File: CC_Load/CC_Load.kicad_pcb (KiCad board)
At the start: 2 copper layers, 160 x 120 mm, 8 parts

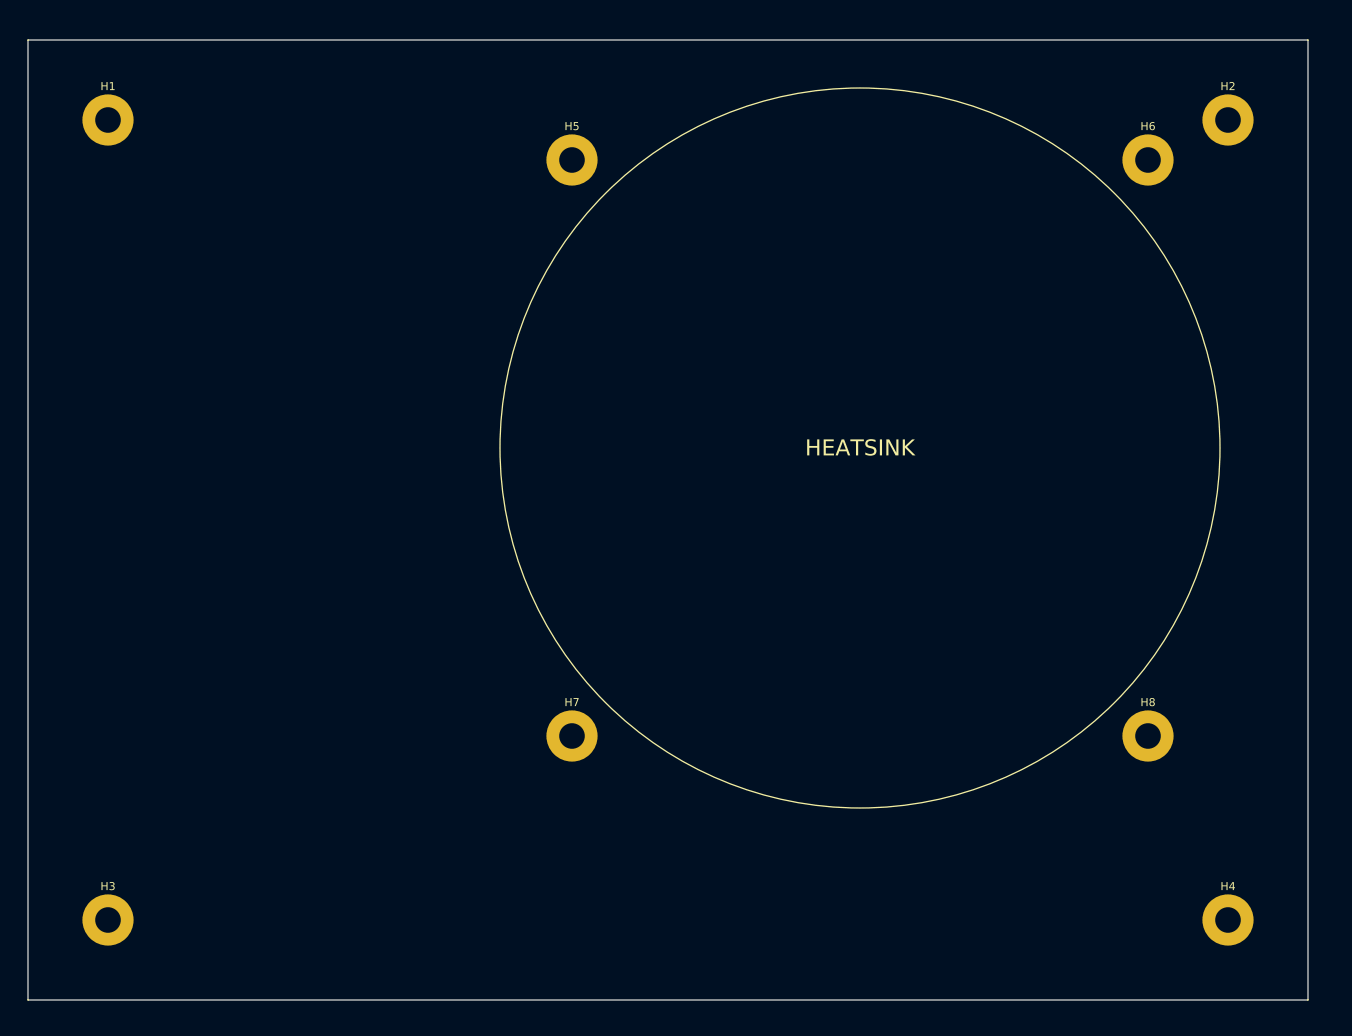
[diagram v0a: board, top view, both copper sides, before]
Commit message: Finished first design for my DIY PCB
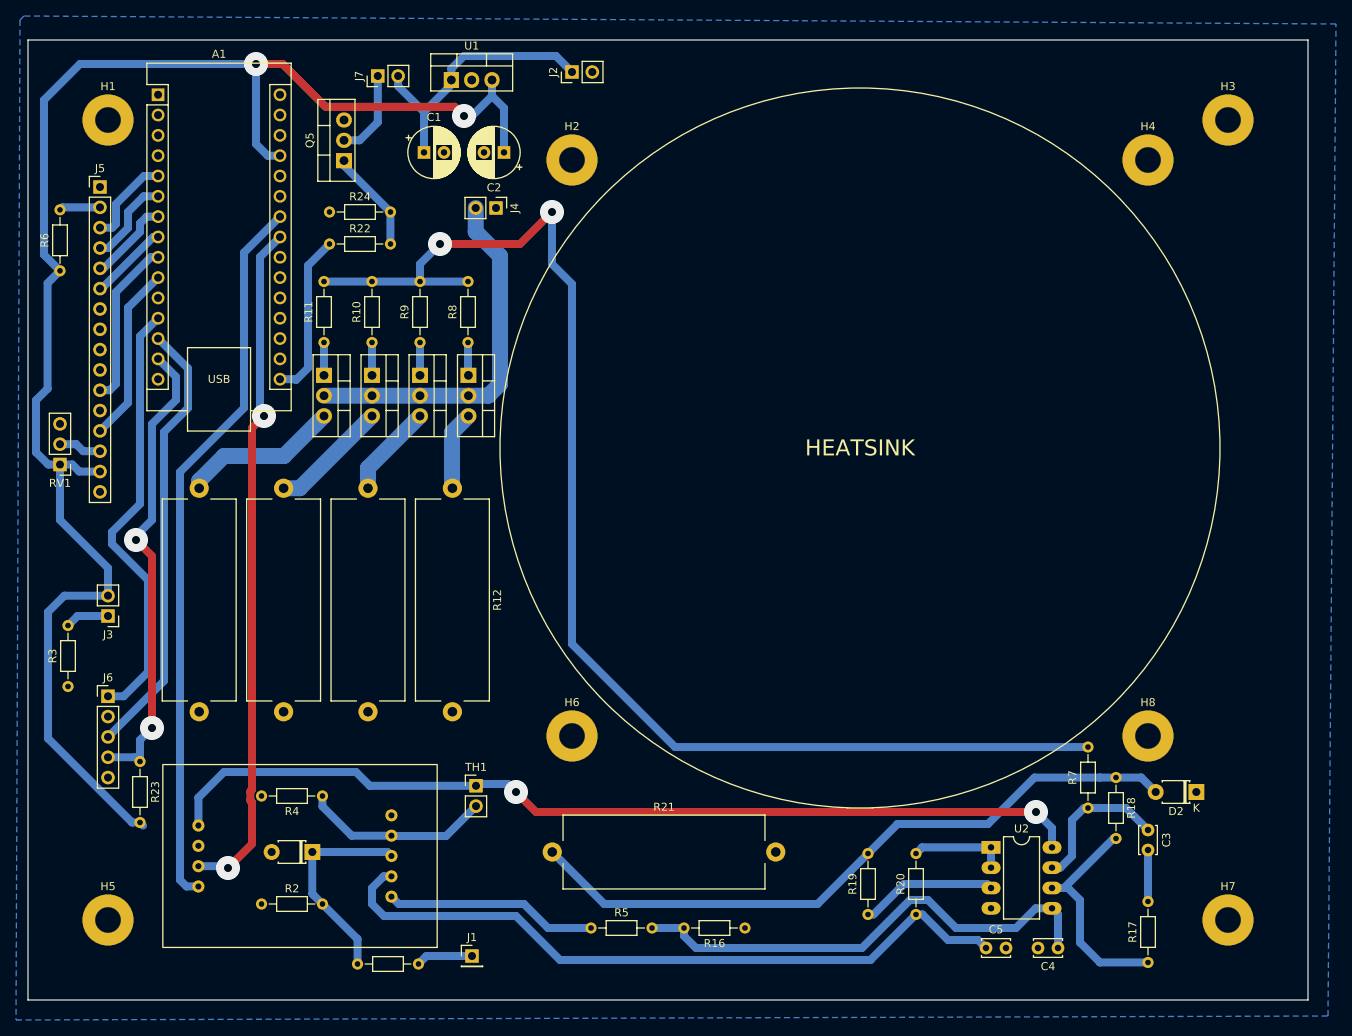
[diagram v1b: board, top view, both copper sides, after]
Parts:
- added A1: Arduino_Nano, Module:Arduino_Nano, F.Cu at (66.3, 36.8)
- added A2: ~, MyFootprintLibrary:ADC_DAC_Board, F.Cu at (84.0, 132.0)
- added C1: 100uF, Capacitor_THT:CP_Radial_D6.3mm_P2.50mm, F.Cu at (99.5, 44.1)
- added C2: 100uF, Capacitor_THT:CP_Radial_D6.3mm_P2.50mm, F.Cu at (109.5, 44.1)
- added C3: 1n, Capacitor_THT:C_Disc_D3.4mm_W2.1mm_P2.50mm, F.Cu at (190.0, 128.8)
- added C4: 100nF, Capacitor_THT:C_Disc_D3.4mm_W2.1mm_P2.50mm, F.Cu at (178.8, 143.5)
- added C5: 100n, Capacitor_THT:C_Disc_D3.4mm_W2.1mm_P2.50mm, F.Cu at (169.8, 143.5)
- added D1: 5V, Diode_THT:D_T-1_P5.08mm_Horizontal, F.Cu at (85.5, 131.5)
- added D2: D, Diode_THT:D_T-1_P5.08mm_Horizontal, F.Cu at (196.0, 124.0)
- added J1: VoltSense_Conn, Connector_PinHeader_2.54mm:PinHeader_1x01_P2.54mm_Vertical, F.Cu at (105.5, 144.5)
- added J2: PowerInput_Conn, Connector_PinHeader_2.54mm:PinHeader_1x02_P2.54mm_Vertical, F.Cu at (118.0, 34.0)
- added J3: LED_Conn, Connector_PinHeader_2.54mm:PinHeader_1x02_P2.54mm_Vertical, F.Cu at (60.0, 102.0)
- added J4: Load_Conn, Connector_PinHeader_2.54mm:PinHeader_1x02_P2.54mm_Vertical, F.Cu at (108.5, 51.0)
- added J5: 16x2_LCD_Conn, Connector_PinHeader_2.54mm:PinHeader_1x16_P2.54mm_Vertical, F.Cu at (59.0, 48.4)
- added J6: RotEnc_Conn, Connector_PinHeader_2.54mm:PinHeader_1x05_P2.54mm_Vertical, F.Cu at (60.0, 112.0)
- added J7: Fan_Conn, Connector_PinHeader_2.54mm:PinHeader_1x02_P2.54mm_Vertical, F.Cu at (93.7, 34.5)
- added Q1: IRLZ44N, Package_TO_SOT_THT:TO-220-3_Vertical, F.Cu at (105.1, 71.9)
- added Q2: IRLZ44N, Package_TO_SOT_THT:TO-220-3_Vertical, F.Cu at (99.0, 71.9)
- added Q3: IRLZ44N, Package_TO_SOT_THT:TO-220-3_Vertical, F.Cu at (93.0, 71.9)
- added Q4: IRLZ44N, Package_TO_SOT_THT:TO-220-3_Vertical, F.Cu at (87.0, 71.9)
- added Q5: IRLZ44N, Package_TO_SOT_THT:TO-220-3_Vertical, F.Cu at (89.5, 45.1)
- added R1: 39k, Resistor_THT:R_Axial_DIN0204_L3.6mm_D1.6mm_P7.62mm_Horizontal, F.Cu at (91.2, 145.5)
- added R10: 100R, Resistor_THT:R_Axial_DIN0204_L3.6mm_D1.6mm_P7.62mm_Horizontal, F.Cu at (93.0, 67.8)
- added R11: 100R, Resistor_THT:R_Axial_DIN0204_L3.6mm_D1.6mm_P7.62mm_Horizontal, F.Cu at (87.0, 67.8)
- added R12: 0.1R, Resistor_THT:R_Axial_Power_L25.0mm_W9.0mm_P27.94mm, F.Cu at (103.0, 86.0)
- added R13: 0.1R, Resistor_THT:R_Axial_Power_L25.0mm_W9.0mm_P27.94mm, F.Cu at (92.5, 86.0)
- added R14: 0.1R, Resistor_THT:R_Axial_Power_L25.0mm_W9.0mm_P27.94mm, F.Cu at (82.0, 86.0)
- added R15: 0.1R, Resistor_THT:R_Axial_Power_L25.0mm_W9.0mm_P27.94mm, F.Cu at (71.4, 86.0)
- added R16: 1k, Resistor_THT:R_Axial_DIN0204_L3.6mm_D1.6mm_P7.62mm_Horizontal, F.Cu at (139.6, 141.0)
- added R17: 1k, Resistor_THT:R_Axial_DIN0204_L3.6mm_D1.6mm_P7.62mm_Horizontal, F.Cu at (190.0, 145.3)
- added R18: 10k, Resistor_THT:R_Axial_DIN0204_L3.6mm_D1.6mm_P7.62mm_Horizontal, F.Cu at (186.0, 122.2)
- added R19: 10k, Resistor_THT:R_Axial_DIN0204_L3.6mm_D1.6mm_P7.62mm_Horizontal, F.Cu at (155.0, 139.3)
- added R2: 10k, Resistor_THT:R_Axial_DIN0204_L3.6mm_D1.6mm_P7.62mm_Horizontal, F.Cu at (79.2, 138.0)
- added R20: 100R, Resistor_THT:R_Axial_DIN0204_L3.6mm_D1.6mm_P7.62mm_Horizontal, F.Cu at (161.0, 139.3)
- added R21: 0.1R, Resistor_THT:R_Axial_Power_L25.0mm_W9.0mm_P27.94mm, F.Cu at (115.5, 131.5)
- added R22: 220R, Resistor_THT:R_Axial_DIN0204_L3.6mm_D1.6mm_P7.62mm_Horizontal, F.Cu at (87.7, 55.5)
- added R23: 10k, Resistor_THT:R_Axial_DIN0204_L3.6mm_D1.6mm_P7.62mm_Horizontal, F.Cu at (64.0, 120.2)
- added R24: 10k, Resistor_THT:R_Axial_DIN0204_L3.6mm_D1.6mm_P7.62mm_Horizontal, F.Cu at (87.7, 51.5)
- added R3: 220R, Resistor_THT:R_Axial_DIN0204_L3.6mm_D1.6mm_P7.62mm_Horizontal, F.Cu at (55.0, 110.8)
- added R4: 10k, Resistor_THT:R_Axial_DIN0204_L3.6mm_D1.6mm_P7.62mm_Horizontal, F.Cu at (86.8, 124.5)
- added R5: 10k, Resistor_THT:R_Axial_DIN0204_L3.6mm_D1.6mm_P7.62mm_Horizontal, F.Cu at (120.4, 141.0)
- added R6: 470R, Resistor_THT:R_Axial_DIN0204_L3.6mm_D1.6mm_P7.62mm_Horizontal, F.Cu at (54.0, 58.9)
- added R7: 100R, Resistor_THT:R_Axial_DIN0204_L3.6mm_D1.6mm_P7.62mm_Horizontal, F.Cu at (182.5, 126.0)
- added R8: 100R, Resistor_THT:R_Axial_DIN0204_L3.6mm_D1.6mm_P7.62mm_Horizontal, F.Cu at (105.0, 67.8)
- added R9: 100R, Resistor_THT:R_Axial_DIN0204_L3.6mm_D1.6mm_P7.62mm_Horizontal, F.Cu at (99.0, 67.8)
- added RV1: 10k, Connector_PinHeader_2.54mm:PinHeader_1x03_P2.54mm_Vertical, F.Cu at (54.0, 83.1)
- added TH1: 10k_NTC, Connector_PinHeader_2.54mm:PinHeader_1x02_P2.54mm_Vertical, F.Cu at (106.0, 123.2)
- added U1: LM7805_TO220, Package_TO_SOT_THT:TO-220-3_Vertical, F.Cu at (102.9, 35.0)
- added U2: LM358, Package_DIP:DIP-8_W7.62mm_LongPads, F.Cu at (170.4, 130.9)
- renumbered H5 to H2, H2 to H3, H6 to H4, H3 to H5, H7 to H6, H4 to H7
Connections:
- H1 pad 1: unconnected-(H1-Pad1) -> GND
- H2 pad 1: unconnected-(H5-Pad1) -> GND
- H3 pad 1: unconnected-(H2-Pad1) -> GND
- H4 pad 1: unconnected-(H6-Pad1) -> GND
- H5 pad 1: unconnected-(H3-Pad1) -> GND
- H6 pad 1: unconnected-(H7-Pad1) -> GND
- H7 pad 1: unconnected-(H4-Pad1) -> GND
- H8 pad 1: unconnected-(H8-Pad1) -> GND
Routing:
- net +5V: track 0.00 -> 316.6 mm, vias 0 -> 4
- net Net-(R10-Pad2): track 0.00 -> 164.3 mm, vias 0 -> 2
- net Net-(A1-SCL/A5): track 0.00 -> 90.7 mm
- net curr_sense: track 0.00 -> 88.8 mm
- net Net-(A1-SDA/A4): track 0.00 -> 86.0 mm, vias 0 -> 2
- net Net-(D2-A): track 0.00 -> 85.4 mm
- net Net-(U2B-+): track 0.00 -> 61.8 mm
- net Net-(A1-MOSI): track 0.00 -> 59.0 mm, vias 0 -> 2
- net Net-(A1-D10): track 0.00 -> 55.5 mm
- net Net-(A1-D9): track 0.00 -> 54.7 mm
- net Net-(J4-Pin_2): track 0.00 -> 45.9 mm
- net +12V: track 0.00 -> 34.3 mm
- net Net-(U2B--): track 0.00 -> 29.5 mm
- net curr_set: track 0.00 -> 26.6 mm
- net volt_sense: track 0.00 -> 26.4 mm
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- added copper zone on B.Cu, net GND

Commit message: Changed PCB design, will order from JLCPCB
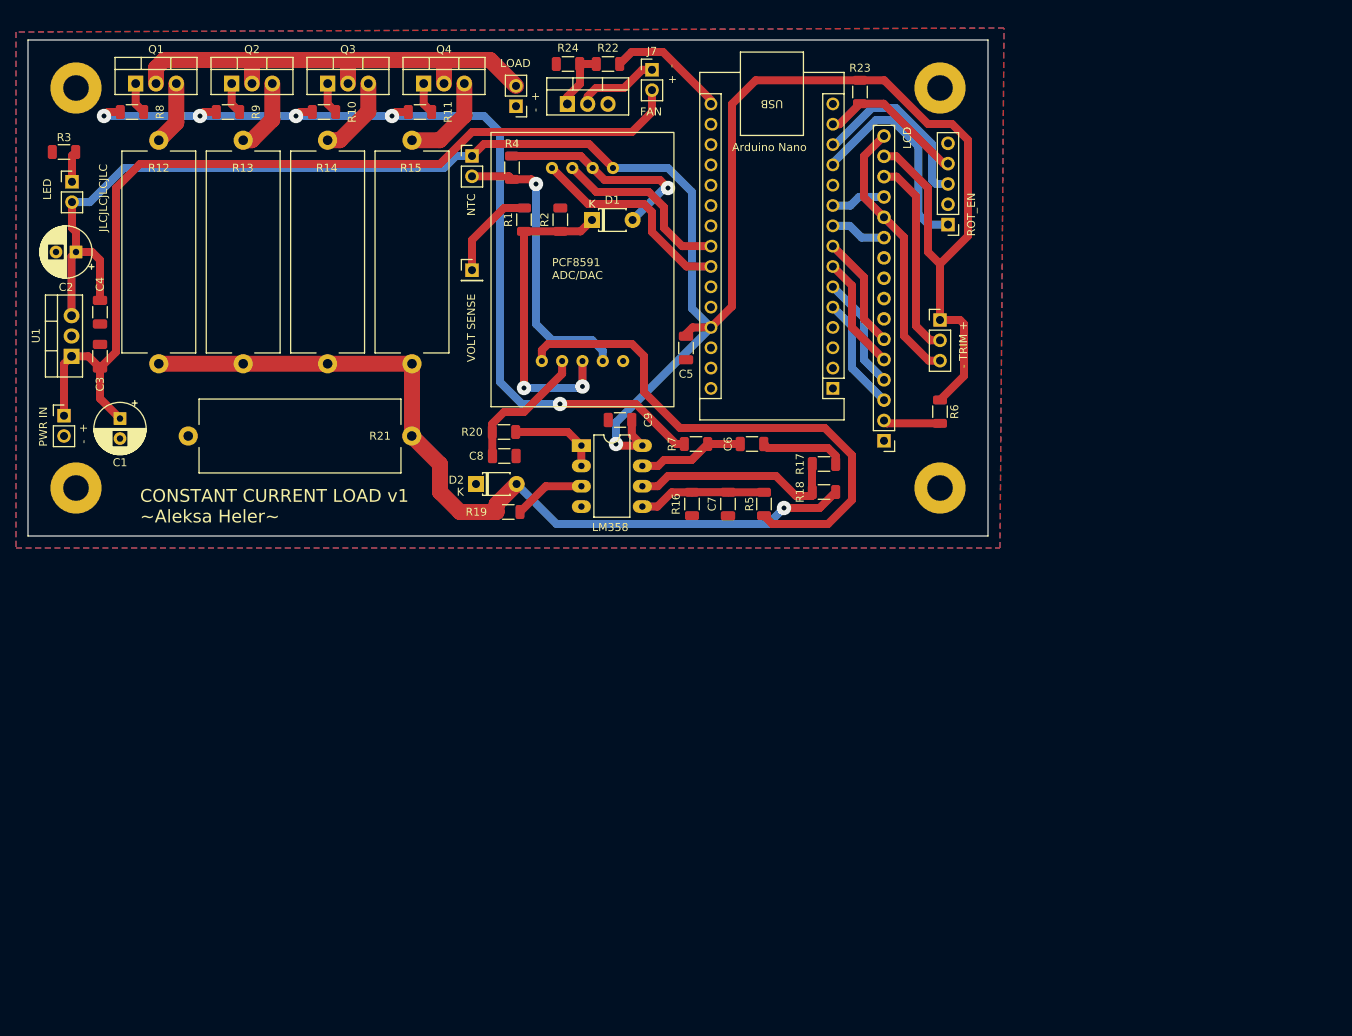
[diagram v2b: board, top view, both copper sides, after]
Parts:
- removed H5, H6, H7, H8: MountingHole_Pad, MountingHole:MountingHole_3.2mm_M3_Pad
- added C6: 1nF, Capacitor_SMD:C_1206_3216Metric, F.Cu at (140.5, 80.5)
- added C7: 100nF, Capacitor_SMD:C_1206_3216Metric, F.Cu at (137.5, 88.0)
- added C8: 100n, Capacitor_SMD:C_1206_3216Metric, F.Cu at (109.5, 82.0)
- added C9: 100nF, Capacitor_SMD:C_1206_3216Metric, F.Cu at (124.0, 77.5)
- C3: value 1n -> 100nF; footprint Capacitor_THT:C_Disc_D3.4mm_W2.1mm_P2.50mm -> Capacitor_SMD:C_1206_3216Metric
- C4: footprint Capacitor_THT:C_Disc_D3.4mm_W2.1mm_P2.50mm -> Capacitor_SMD:C_1206_3216Metric
- C5: value 100n -> 100nF; footprint Capacitor_THT:C_Disc_D3.4mm_W2.1mm_P2.50mm -> Capacitor_SMD:C_1206_3216Metric
- R1: value 39k -> 47k; footprint Resistor_THT:R_Axial_DIN0204_L3.6mm_D1.6mm_P7.62mm_Horizontal -> Resistor_SMD:R_1206_3216Metric
- R10, R11, R16, R17, R18, R19, R2, R20, R22, R23, R24, R3, R4, R5, R6, R7, R8, R9: footprint Resistor_THT:R_Axial_DIN0204_L3.6mm_D1.6mm_P7.62mm_Horizontal -> Resistor_SMD:R_1206_3216Metric
- moved H3 151.2 mm to (56.0, 86.0)
- moved C3 143.8 mm to (59.0, 69.5), turned to 90 degrees
- moved C4 143.7 mm to (59.0, 64.0), turned to -90 degrees
- moved R23 122.9 mm to (154.0, 36.5), turned to 90 degrees
- moved J6 120.4 mm to (165.0, 53.1), turned to 180 degrees
- moved RV1 111.5 mm to (164.0, 65.0), turned to 0 degrees
- moved R6 111.4 mm to (164.0, 76.5), turned to -90 degrees
- moved J5 103.0 mm to (157.0, 80.1), turned to 180 degrees
- moved D2 97.9 mm to (106.0, 85.5), turned to 0 degrees
- moved R1 95.3 mm to (112.0, 52.5), turned to 90 degrees
- moved R2 93.3 mm to (116.5, 52.5), turned to -90 degrees
- moved A1 92.0 mm to (150.6, 73.5), turned to 180 degrees
- moved D1 86.4 mm to (120.5, 52.5), turned to 0 degrees
- moved J1 85.7 mm to (105.5, 58.8)
- moved C5 83.9 mm to (132.2, 68.5), turned to -90 degrees
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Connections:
- C3 pad 1: Net-(C3-Pad1) -> +12V
- C3 pad 2: Net-(C3-Pad2) -> GND
- C4 pad 1: Net-(U2B-+) -> +5V
- C5 pad 1: curr_sense -> +5V
- R17 pad 2: Net-(C3-Pad2) -> Net-(C6-Pad2)
- R7 pad 1: Net-(C3-Pad1) -> Net-(C6-Pad1)
- U2 pad 7: Net-(C3-Pad1) -> Net-(C6-Pad1)
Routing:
- net +12V: track 34.3 -> 116.3 mm
- net curr_sense: track 88.8 -> 17.0 mm
- net Net-(A1-SCL/A5): track 90.7 -> 26.4 mm
- net Net-(A1-SDA/A4): track 86.0 -> 22.9 mm, vias 2 -> 0
- net GND: track 0.00 -> 61.1 mm, vias 0 -> 1
- net Net-(R10-Pad2): track 164.3 -> 116.8 mm, vias 2 -> 5
- net Net-(U2B-+): track 61.8 -> 16.0 mm
- net +5V: track 316.6 -> 272.3 mm, vias 4 -> 1
- net curr_set: track 26.6 -> 67.1 mm
- net Net-(A1-MOSI): track 59.0 -> 18.6 mm, vias 2 -> 0
- net Net-(A1-D10): track 55.5 -> 22.9 mm
- net Net-(A1-D9): track 54.7 -> 27.2 mm
- net Net-(D2-A): track 85.4 -> 105.4 mm, vias 0 -> 1
- net Net-(J5-Pin_14): track 5.38 -> 25.0 mm
- net Net-(C3-Pad1): track 18.9 -> 0.00 mm
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- added copper zone on F.Cu, net GND
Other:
- board size 160 x 120 mm -> 120 x 62 mm
- board text added: "- +"
- board text added: "- TRIM +"
- board text added: "Arduino Nano"
- board text added: "CONSTANT CURRENT LOAD v1 ~Aleksa Heler~"
- board text added: "FAN"
- board text added: "JLCJLCJLCJLC"
- board text added: "LCD"
- board text added: "LED"
- board text added: "LM358"
- board text added: "LOAD"
- board text added: "NTC"
- board text added: "PCF8591 ADC/DAC"
- board text added: "PWR IN"
- board text added: "ROT_EN"
- board text added: "VOLT SENSE"
- board text removed: "HEATSINK"
